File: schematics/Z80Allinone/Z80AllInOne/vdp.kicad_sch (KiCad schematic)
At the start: 25 parts, among them J3 COMP_VIDEOUT, Q2 2N3904, U10 74LS574, U11 AS6C62256-55PCN, U16 74LS32, U17 74HC04, U7 TMS9918A, U8 74LS574, U9 74LS574, Y2 10.73MHz

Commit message: Latest modifications of All-in-one PCB
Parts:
- removed D5: 1N4148, Diode_THT:D_DO-35_SOD27_P7.62mm_Horizontal, symbol Diode:1N4148
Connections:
- net VDP_INT: now also U7.16 (~{INT})
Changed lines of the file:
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@@
     (stroke (width 0) (type default) (color 0 0 0 0))
   )
-  (wire (pts (xy 44.45 93.98) (xy 52.07 93.98))
+  (wire (pts (xy 30.48 93.98) (xy 52.07 93.98))
     (stroke (width 0) (type default) (color 0 0 0 0))
   )
@@
   )
   (wire (pts (xy 261.62 72.39) (xy 271.78 72.39))
-    (stroke (width 0) (type default) (color 0 0 0 0))
-  )
-  (wire (pts (xy 30.48 93.98) (xy 36.83 93.98))
     (stroke (width 0) (type default) (color 0 0 0 0))
   )
@@
     (pin "1")
   )
-  (symbol (lib_id "Diode:1N4148") (at 40.64 93.98 180) (unit 1)
-    (in_bom yes) (on_board yes)
-    (property "Reference" "D5" (id 0) (at 40.64 88.9 0))
-    (property "Value" "1N4148" (id 1) (at 40.64 91.44 0))
-    (property "Footprint" "Diode_THT:D_DO-35_SOD27_P7.62mm_Horizontal" (id 2) (at 40.64 89.535 0)
-      (effects (font (size 1.27 1.27)) hide)
-    )
-    (property "Datasheet" "https://assets.nexperia.com/documents/data-sheet/1N4148_1N4448.pdf" (id 3) (at 40.64 93.98 0)
-      (effects (font (size 1.27 1.27)) hide)
-    )
-    (pin "1")
-    (pin "2")
-  )
   (symbol (lib_id "Transistor_BJT:2N3904") (at 36.83 168.91 0) (unit 1)

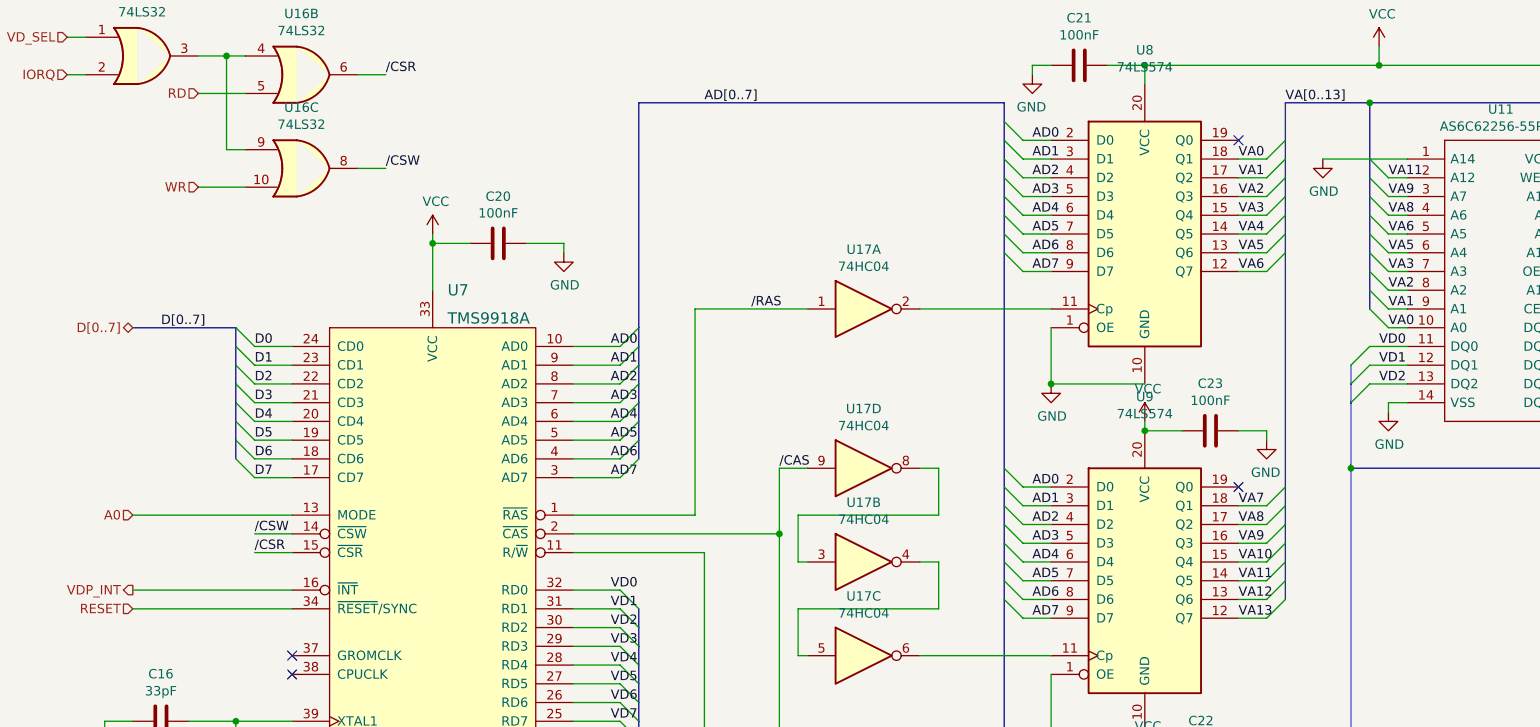
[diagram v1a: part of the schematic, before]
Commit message: Latest changes and replace CTC for 8253 PIT
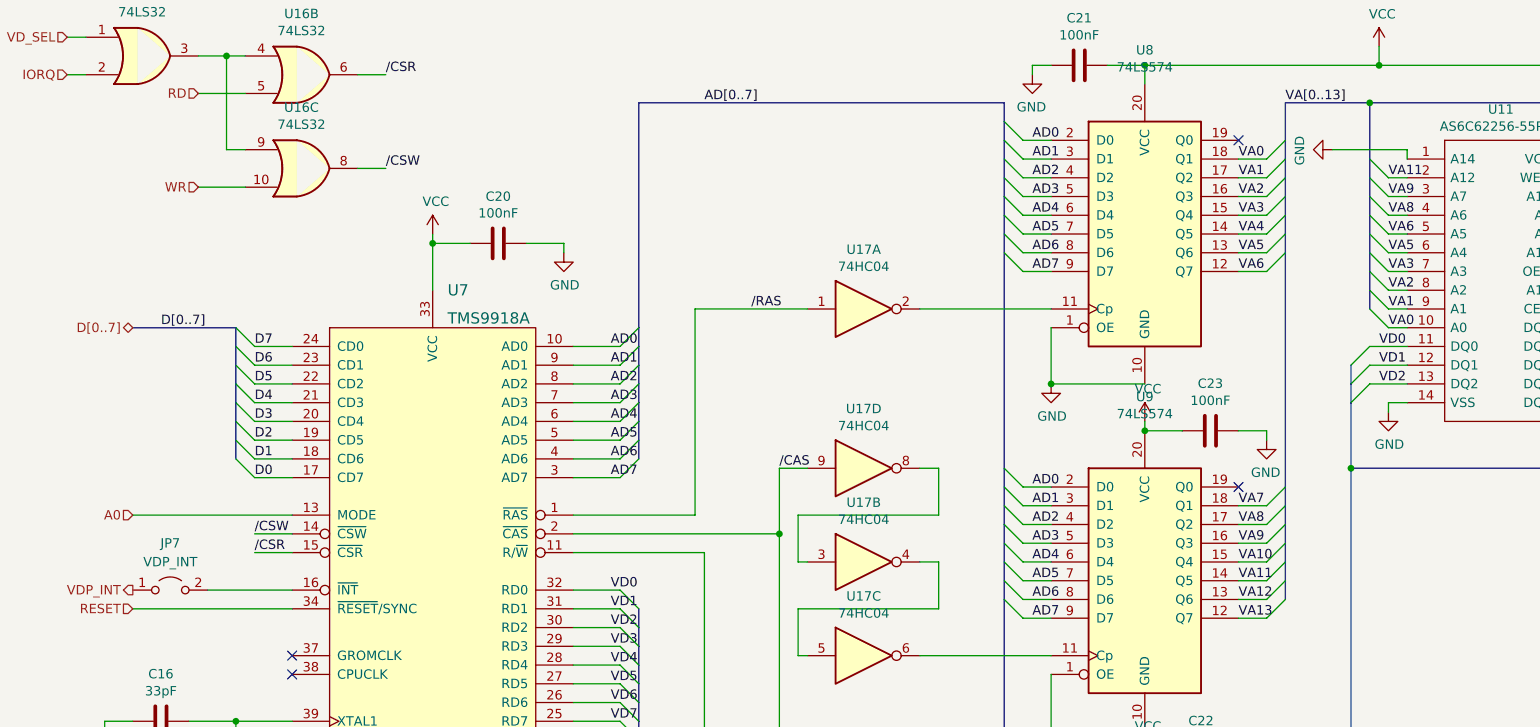
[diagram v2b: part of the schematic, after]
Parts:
- added JP7: VDP_INT, Connector_PinHeader_2.54mm:PinHeader_1x02_P2.54mm_Vertical, symbol Jumper:Jumper_2_Open
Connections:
- net D0: now also U7.17 (CD7); no longer U7.24 (CD0)
- net D1: now also U7.18 (CD6); no longer U7.23 (CD1)
- net D2: now also U7.19 (CD5); no longer U7.22 (CD2)
- net D3: now also U7.20 (CD4); no longer U7.21 (CD3)
- net D4: now also U7.21 (CD3); no longer U7.20 (CD4)
- net D5: now also U7.22 (CD2); no longer U7.19 (CD5)
- net D6: now also U7.23 (CD1); no longer U7.18 (CD6)
- net D7: now also U7.24 (CD0); no longer U7.17 (CD7)
- net VDP_INT: now also JP7.1 (A); no longer U7.16 (~{INT})
- new net: JP7.2 (B), U7.16 (~{INT})
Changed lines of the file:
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@@
     (stroke (width 0) (type default) (color 0 0 0 0))
   )
-  (wire (pts (xy 30.48 93.98) (xy 52.07 93.98))
+  (wire (pts (xy 40.64 93.98) (xy 52.07 93.98))
     (stroke (width 0) (type default) (color 0 0 0 0))
   )
@@
     (stroke (width 0) (type default) (color 0 0 0 0))
   )
+  (wire (pts (xy 203.2 35.56) (xy 203.2 34.29))
+    (stroke (width 0) (type default) (color 0 0 0 0))
+  )
   (wire (pts (xy 137.16 102.87) (xy 154.94 102.87))
     (stroke (width 0) (type default) (color 0 0 0 0))
@@
     (stroke (width 0) (type default) (color 0 0 0 0))
   )
-  (wire (pts (xy 198.12 35.56) (xy 203.2 35.56))
-    (stroke (width 0) (type default) (color 0 0 0 0))
-  )
   (wire (pts (xy 200.66 50.8) (xy 203.2 50.8))
     (stroke (width 0) (type default) (color 0 0 0 0))
@@
     (stroke (width 0) (type default) (color 0 0 0 0))
   )
+  (wire (pts (xy 203.2 34.29) (xy 193.04 34.29))
+    (stroke (width 0) (type default) (color 0 0 0 0))
+  )
   (wire (pts (xy 228.6 48.26) (xy 232.41 48.26))
     (stroke (width 0) (type default) (color 0 0 0 0))
@@
     (stroke (width 0) (type default) (color 0 0 0 0))
   )
-  (wire (pts (xy 191.77 35.56) (xy 198.12 35.56))
-    (stroke (width 0) (type default) (color 0 0 0 0))
-  )
   (bus (pts (xy 186.69 27.94) (xy 186.69 33.02))
     (stroke (width 0) (type default) (color 0 0 0 0))
@@
     (stroke (width 0) (type default) (color 0 0 0 0))
   )
+  (label "D5" (at 46.99 66.04 0)
+    (effects (font (size 1.27 1.27)) (justify left bottom))
+  )
   (label "VA5" (at 180.34 48.26 0)
     (effects (font (size 1.27 1.27)) (justify left bottom))
@@
     (effects (font (size 1.27 1.27)) (justify left bottom))
   )
+  (label "D4" (at 46.99 68.58 0)
+    (effects (font (size 1.27 1.27)) (justify left bottom))
+  )
   (label "VD7" (at 228.6 58.42 0)
     (effects (font (size 1.27 1.27)) (justify left bottom))
@@
     (effects (font (size 1.27 1.27)) (justify left bottom))
   )
-  (label "D0" (at 46.99 60.96 0)
-    (effects (font (size 1.27 1.27)) (justify left bottom))
-  )
   (label "VD5" (at 228.6 63.5 0)
     (effects (font (size 1.27 1.27)) (justify left bottom))
@@
     (effects (font (size 1.27 1.27)) (justify left bottom))
   )
+  (label "D2" (at 46.99 73.66 0)
+    (effects (font (size 1.27 1.27)) (justify left bottom))
+  )
   (label "VD2" (at 199.39 66.04 0)
     (effects (font (size 1.27 1.27)) (justify left bottom))
@@
     (effects (font (size 1.27 1.27)) (justify left bottom))
   )
-  (label "D6" (at 46.99 76.2 0)
-    (effects (font (size 1.27 1.27)) (justify left bottom))
-  )
   (label "{slash}CSW" (at 46.99 86.36 0)
     (effects (font (size 1.27 1.27)) (justify left bottom))
   )
-  (label "D2" (at 46.99 66.04 0)
+  (label "D7" (at 46.99 60.96 0)
     (effects (font (size 1.27 1.27)) (justify left bottom))
   )
@@
     (effects (font (size 1.27 1.27)) (justify left bottom))
   )
+  (label "D3" (at 46.99 71.12 0)
+    (effects (font (size 1.27 1.27)) (justify left bottom))
+  )
   (label "VA8" (at 180.34 85.09 0)
     (effects (font (size 1.27 1.27)) (justify left bottom))
@@
     (effects (font (size 1.27 1.27)) (justify left bottom))
   )
+  (label "D1" (at 46.99 76.2 0)
+    (effects (font (size 1.27 1.27)) (justify left bottom))
+  )
   (label "AD[0..7]" (at 107.95 27.94 0)
     (effects (font (size 1.27 1.27)) (justify left bottom))
@@
     (effects (font (size 1.27 1.27)) (justify left bottom))
   )
-  (label "D7" (at 46.99 78.74 0)
-    (effects (font (size 1.27 1.27)) (justify left bottom))
-  )
   (label "VA13" (at 229.87 40.64 0)
     (effects (font (size 1.27 1.27)) (justify left bottom))
@@
     (effects (font (size 1.27 1.27)) (justify left bottom))
   )
+  (label "D6" (at 46.99 63.5 0)
+    (effects (font (size 1.27 1.27)) (justify left bottom))
+  )
   (label "VA7" (at 180.34 82.55 0)
     (effects (font (size 1.27 1.27)) (justify left bottom))
@@
     (effects (font (size 1.27 1.27)) (justify left bottom))
   )
-  (label "D3" (at 46.99 68.58 0)
-    (effects (font (size 1.27 1.27)) (justify left bottom))
-  )
   (label "VD0" (at 190.5 127 0)
     (effects (font (size 1.27 1.27)) (justify left bottom))
@@
     (effects (font (size 1.27 1.27)) (justify left bottom))
   )
-  (label "D4" (at 46.99 71.12 0)
-    (effects (font (size 1.27 1.27)) (justify left bottom))
-  )
   (label "VD6" (at 95.25 109.22 0)
     (effects (font (size 1.27 1.27)) (justify left bottom))
@@
     (effects (font (size 1.27 1.27)) (justify left bottom))
   )
-  (label "D5" (at 46.99 73.66 0)
-    (effects (font (size 1.27 1.27)) (justify left bottom))
-  )
   (label "AD4" (at 95.25 71.12 0)
     (effects (font (size 1.27 1.27)) (justify left bottom))
@@
     (effects (font (size 1.27 1.27)) (justify left bottom))
   )
-  (label "D1" (at 46.99 63.5 0)
-    (effects (font (size 1.27 1.27)) (justify left bottom))
-  )
   (label "AD0" (at 95.25 60.96 0)
     (effects (font (size 1.27 1.27)) (justify left bottom))
@@
   )
   (label "AD0" (at 152.4 80.01 0)
+    (effects (font (size 1.27 1.27)) (justify left bottom))
+  )
+  (label "D0" (at 46.99 78.74 0)
     (effects (font (size 1.27 1.27)) (justify left bottom))
   )
@@
     (pin "1")
   )
+  (symbol (lib_id "Jumper:Jumper_2_Open") (at 35.56 93.98 0) (unit 1)
+    (in_bom yes) (on_board yes) (fields_autoplaced)
+    (property "Reference" "JP7" (id 0) (at 35.56 87.63 0))
+    (property "Value" "VDP_INT" (id 1) (at 35.56 90.17 0))
+    (property "Footprint" "Connector_PinHeader_2.54mm:PinHeader_1x02_P2.54mm_Vertical" (id 2) (at 35.56 93.98 0)
+      (effects (font (size 1.27 1.27)) hide)
+    )
+    (property "Datasheet" "~" (id 3) (at 35.56 93.98 0)
+      (effects (font (size 1.27 1.27)) hide)
+    )
+    (pin "1")
+    (pin "2")
+  )
   (symbol (lib_id "74xx:74HC04") (at 129.54 55.88 0) (unit 1)
     (in_bom yes) (on_board yes)
@@
     (pin "3")
   )
-  (symbol (lib_id "power:GND") (at 191.77 35.56 0) (unit 1)
-    (in_bom yes) (on_board yes)
-    (property "Reference" "#PWR0175" (id 0) (at 191.77 41.91 0)
-      (effects (font (size 1.27 1.27)) hide)
-    )
-    (property "Value" "GND" (id 1) (at 191.897 39.9542 0))
-    (property "Footprint" "" (id 2) (at 191.77 35.56 0)
-      (effects (font (size 1.27 1.27)) hide)
-    )
-    (property "Datasheet" "" (id 3) (at 191.77 35.56 0)
-      (effects (font (size 1.27 1.27)) hide)
-    )
+  (symbol (lib_id "power:GND") (at 193.04 34.29 270) (unit 1)
+    (in_bom yes) (on_board yes)
+    (property "Reference" "#PWR0175" (id 0) (at 186.69 34.29 0)
+      (effects (font (size 1.27 1.27)) hide)
+    )
+    (property "Value" "GND" (id 1) (at 188.6458 34.417 0))
+    (property "Footprint" "" (id 2) (at 193.04 34.29 0)
+      (effects (font (size 1.27 1.27)) hide)
+    )
+    (property "Datasheet" "" (id 3) (at 193.04 34.29 0)
+      (effects (font (size 1.27 1.27)) hide)
+    )
